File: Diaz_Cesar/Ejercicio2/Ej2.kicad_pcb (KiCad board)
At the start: 2 copper layers, 40.6 x 61 mm, 15 parts, among them J1 DB9, U1 AMIS42665TJAA1RG, U2 SP3232DC

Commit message: Agrego 3D
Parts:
- moved JP1 2.54 mm to (86.4, 95.2)
- moved G*** 0.63 mm to (102.9, 111.1)
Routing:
- net /Conector y CAN/CAN_P: track 21.2 -> 20.2 mm
- net /Conector y CAN/CAN_N: track 20.7 -> 20.2 mm
- added copper zone on B.Cu, net GND
- added copper zone on F.Cu, net GND
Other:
- board text added: "INDUSTRIA ARGENTINA"

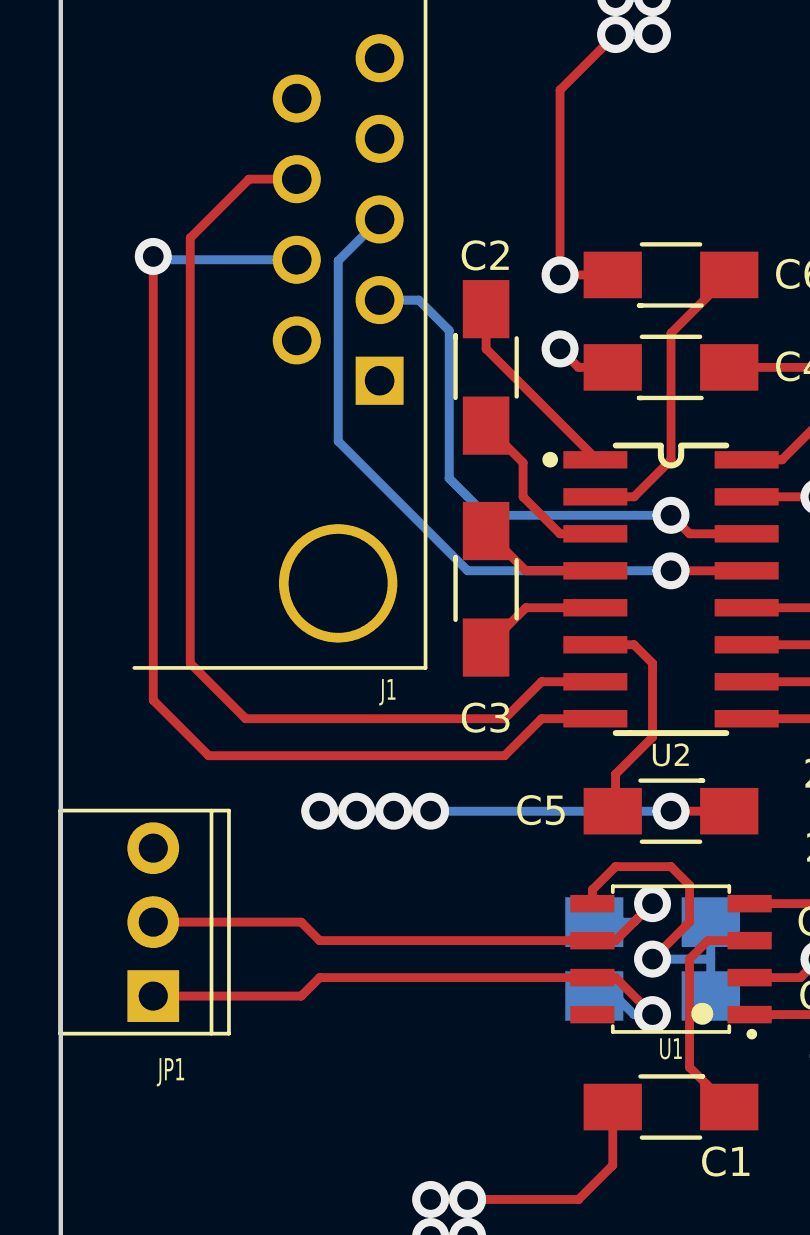
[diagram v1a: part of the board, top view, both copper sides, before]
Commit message: agregado par dif
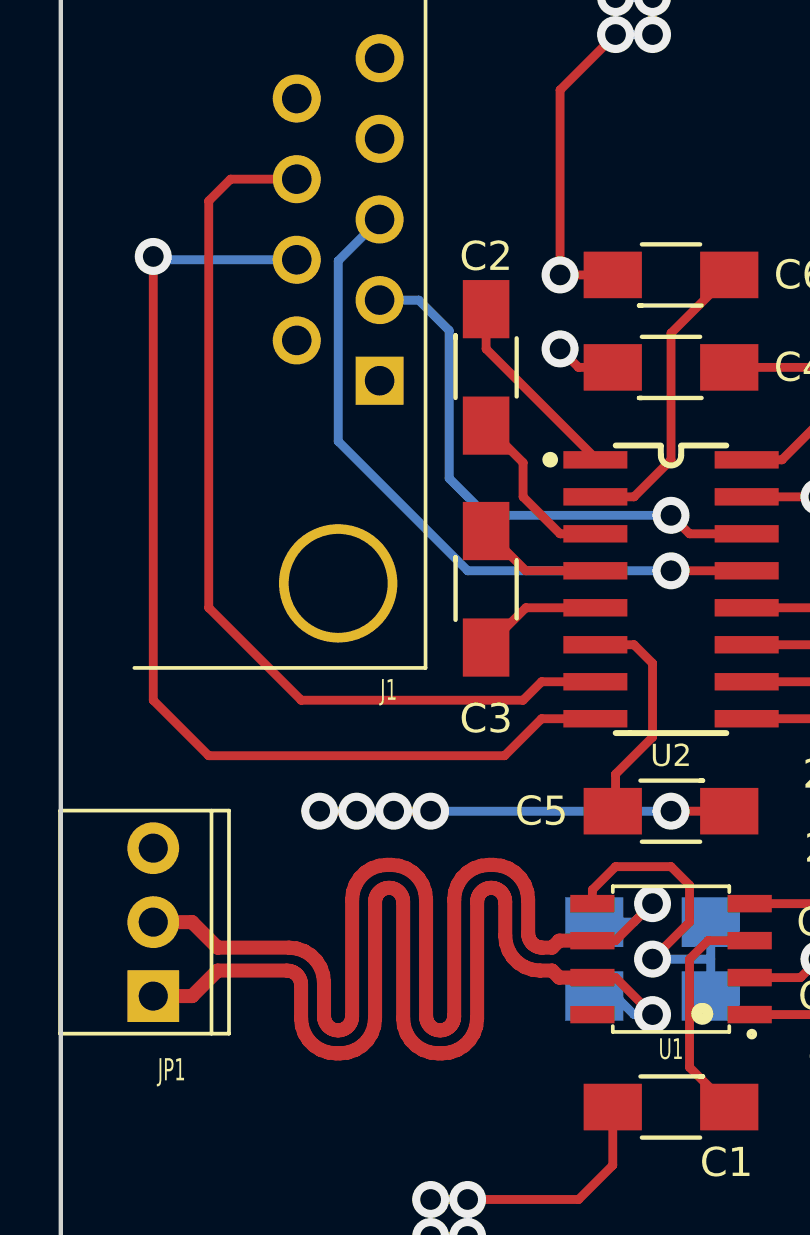
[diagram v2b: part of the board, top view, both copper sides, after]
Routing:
- net /Conector y CAN/CAN_P: track 20.2 -> 39.5 mm
- net /Conector y CAN/CAN_N: track 20.2 -> 39.5 mm
- net Net-(J1-Pad8): track 34.3 -> 32.2 mm
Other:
- board text added: "1 Oz"
- board text added: "1,6mm"
- board text added: "Dielectrico"
- board text added: "L1 Top (Mixed)"
- board text added: "L2 Bottom (Mixed)"
- board text added: "Stack-UP"
- board text added: "Terminacion superficial: ASHL Espesor final aproximado: 1,6mm"
